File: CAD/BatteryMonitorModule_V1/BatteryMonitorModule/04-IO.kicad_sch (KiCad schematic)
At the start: 33 parts, among them J10 J_DISP_SPI, J11 J_UART, J12 J_EXP_B, J13 J_EXP_A, J5 J_FAN, J6 J_FAN_SEL, J7 J_NFC, J8 J_PANEL, Q5 2N7002

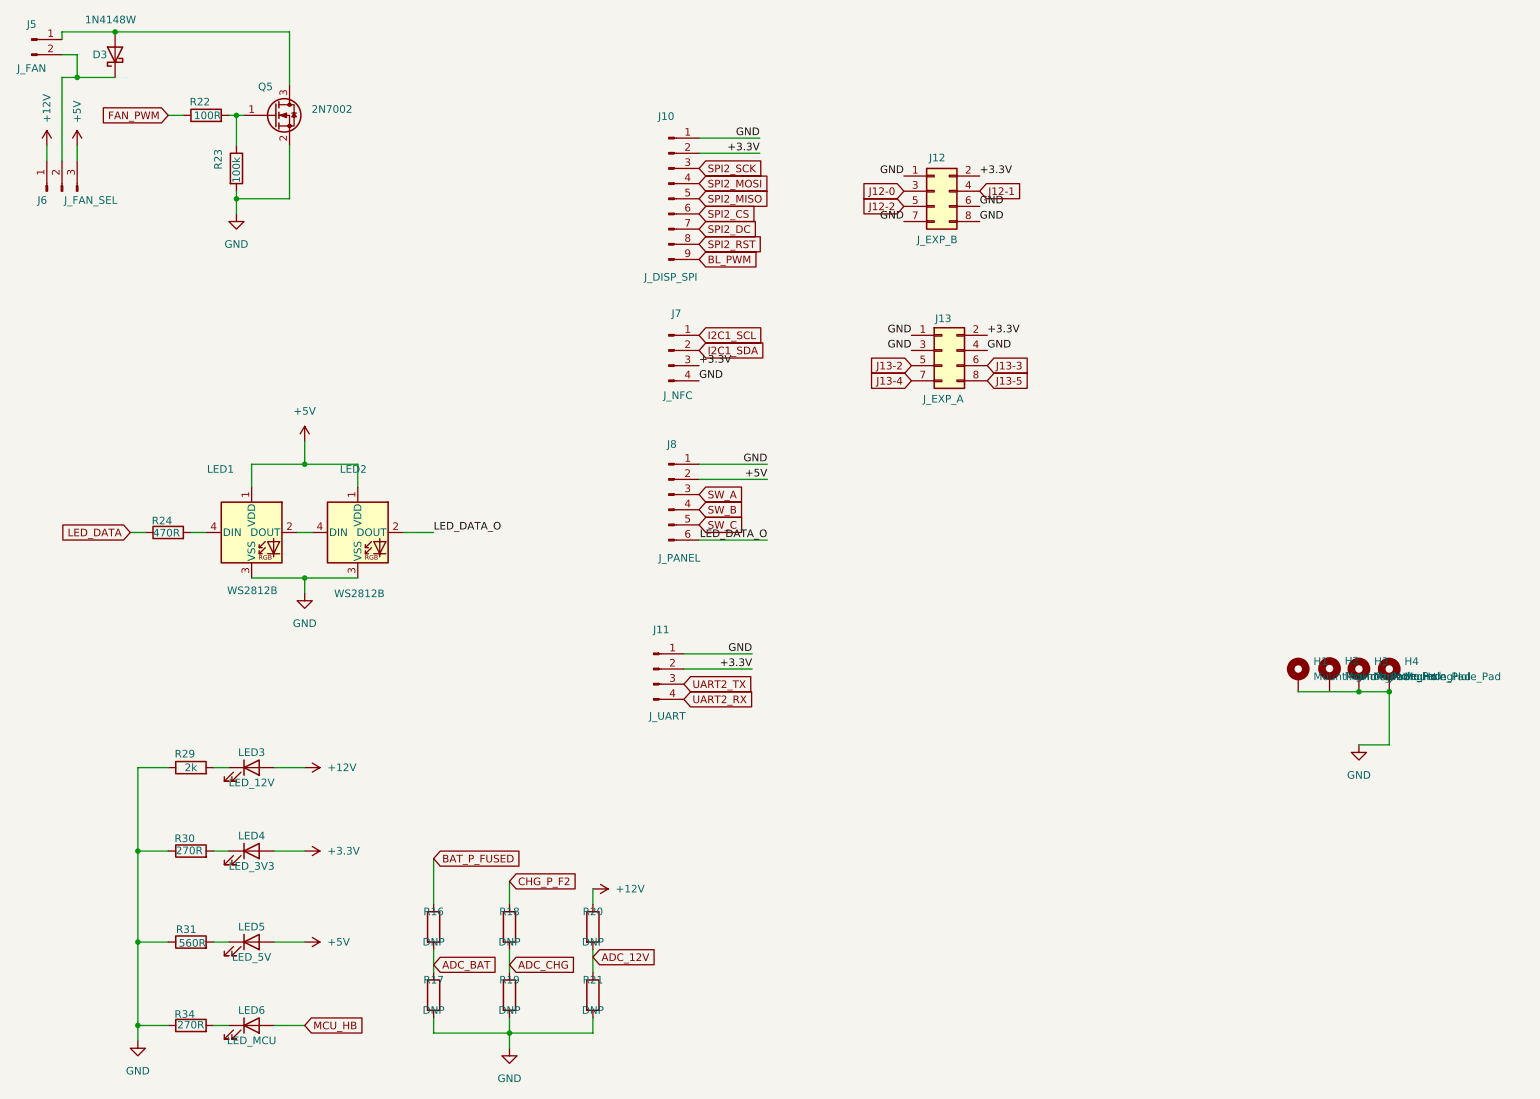
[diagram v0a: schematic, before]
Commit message: V1 schematic rework — PowerPath, PowerSupply, IO updates and custom library additions
Add custom symbols/footprints for Keystone 4966 and AO4407A, and SOIC127P600X175-8N
footprint. Update sym-lib-table to reference new custom library.

Co-Authored-By: Claude Opus 4.7 (1M context) <noreply@anthropic.com>
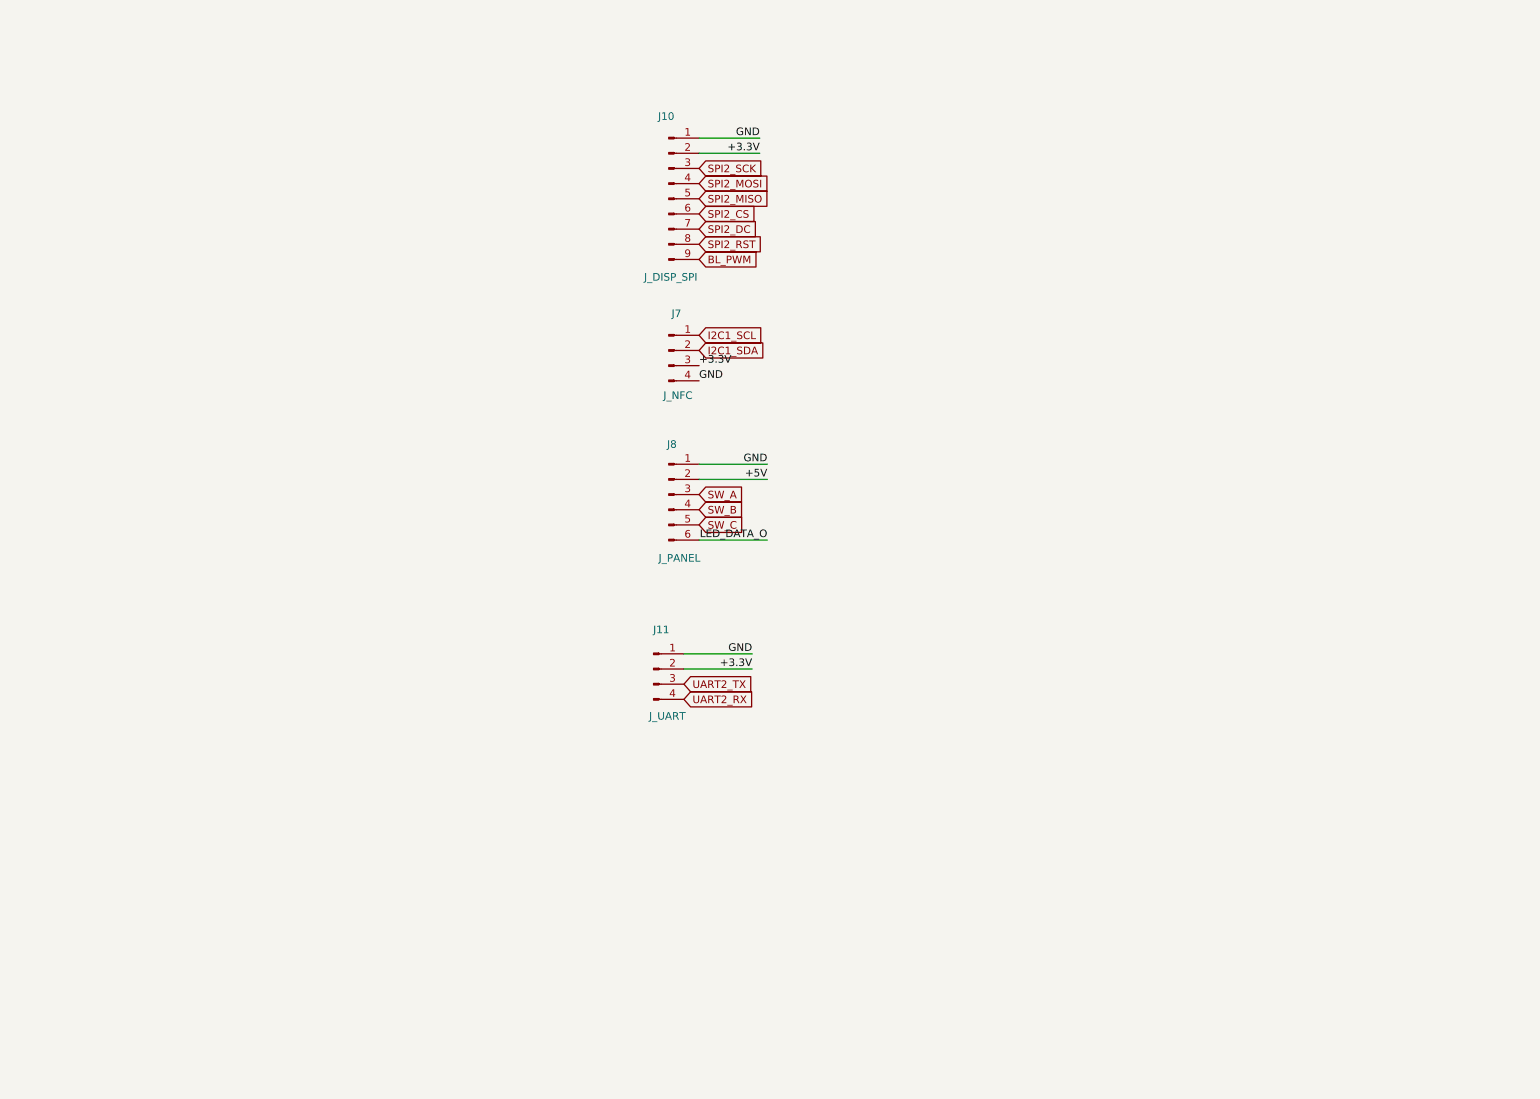
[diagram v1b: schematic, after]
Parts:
- removed D3: 1N4148W, Diode_SMD:D_SOD-123, symbol Device:D_Schottky
- removed H1, H2, H3, H4: MountingHole_Pad, symbol Mechanical:MountingHole_Pad
- removed J12: J_EXP_B, Connector_PinHeader_2.54mm:PinHeader_2x04_P2.54mm_Vertical, symbol Connector_Generic:Conn_02x04_Odd_Even
- removed J13: J_EXP_A, Connector_PinHeader_2.54mm:PinHeader_2x04_P2.54mm_Vertical, symbol Connector_Generic:Conn_02x04_Odd_Even
- removed J5: J_FAN, Connector_PinHeader_2.54mm:PinHeader_1x02_P2.54mm_Vertical, symbol Connector:Conn_01x02_Pin
- removed J6: J_FAN_SEL, Connector_PinHeader_2.54mm:PinHeader_1x03_P2.54mm_Vertical, symbol Connector:Conn_01x03_Pin
- removed LED1, LED2: WS2812B, LED_SMD:LED_WS2812B_PLCC4_5.0x5.0mm_P3.2mm, symbol LED:WS2812B
- removed LED3: LED_12V, LED_SMD:LED_0603_1608Metric, symbol Device:LED
- removed LED4: LED_3V3, LED_SMD:LED_0603_1608Metric, symbol Device:LED
- removed LED5: LED_5V, LED_SMD:LED_0603_1608Metric, symbol Device:LED
- removed LED6: LED_MCU, LED_SMD:LED_0603_1608Metric, symbol Device:LED
- removed Q5: 2N7002, Package_TO_SOT_SMD:SOT-23, symbol Transistor_FET:BSS138
- removed R16, R17, R18, R19, R20, R21: DNP, Resistor_SMD:R_0603_1608Metric, symbol Device:R
- removed R22: 100R, Resistor_SMD:R_0603_1608Metric, symbol Device:R
- removed R23: 100k, Resistor_SMD:R_0603_1608Metric, symbol Device:R
- removed R24: 470R, Resistor_SMD:R_0603_1608Metric, symbol Device:R
- removed R29: 2k, Resistor_SMD:R_0603_1608Metric, symbol Device:R
- removed R30, R34: 270R, Resistor_SMD:R_0603_1608Metric, symbol Device:R
- removed R31: 560R, Resistor_SMD:R_0603_1608Metric, symbol Device:R

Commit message: add QT06ADP83H0000G and UJ20-C USB-C connector symbols/footprints/3D models
Update V1 schematics (PowerPath, MCU, IO, top-level) to incorporate new parts.

Co-Authored-By: Claude Opus 4.7 (1M context) <noreply@anthropic.com>
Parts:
- removed J10: J_DISP_SPI, Connector_JST:JST_XH_B9B-XH-A_1x09_P2.50mm_Vertical, symbol Connector:Conn_01x09_Pin
- removed J11: J_UART, Connector_PinHeader_2.54mm:PinHeader_1x04_P2.54mm_Vertical, symbol Connector:Conn_01x04_Pin
- removed J7: J_NFC, Connector_JST:JST_XH_B4B-XH-A_1x04_P2.50mm_Vertical, symbol Connector:Conn_01x04_Pin
- removed J8: J_PANEL, Connector_JST:JST_XH_B6B-XH-A_1x06_P2.50mm_Vertical, symbol Connector:Conn_01x06_Pin
